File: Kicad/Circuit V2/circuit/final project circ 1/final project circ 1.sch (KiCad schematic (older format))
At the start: 86 parts, among them J1 USB_B_Micro, J10 Conn_01x02_Female, J11 Conn_01x02_Female, J2 Conn_01x01_Female, J3 Conn_01x04_Female, J4 Conn_01x04_Female, J5 Conn_01x03_Female, J6 Conn_01x03_Female, J7 Conn_01x04_Female, J8 Conn_01x02_Female, J9 Conn_01x02_Female, Q1 FDD770N15A, Q2 FDD770N15A, Q3 FDD770N15A, Q4 SS8050-G, Q5 SS8050-G, Q6 2SC1945, SW1 SW_Push, SW2 SW_Push, U1 LTC3895IFE, U2 CP2102N-A01-GQFN28, U3 AZ1117-3.3, U4 USBLC6-4, U5 AZ1117-3.3, U6 ESP32-WROOM-32D, U7 SRD-S-112DM, U8 L2293QTR

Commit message: pcb progress
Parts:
- D6: symbol final-project-circ-1-rescue:PMEG3005EJ-Diode-final-project-circ-1-rescue -> final-project-circ-1-rescue:PMEG3005EJ-Diode-final-project-circ-1-rescue-final-project-circ-1-rescue
- J1: symbol final-project-circ-1-rescue:USB_B_Micro-Connector-final-project-circ-1-rescue -> final-project-circ-1-rescue:USB_B_Micro-Connector-final-project-circ-1-rescue-final-project-circ-1-rescue
- Q1, Q2, Q3: symbol final-project-circ-1-rescue:FDD770N15A-POWSYMBOLS-SDPowSupply-rescue-final-project-circ-1-rescue -> final-project-circ-1-rescue:FDD770N15A-POWSYMBOLS-SDPowSupply-rescue-final-project-circ-1-rescue-final-project-circ-1-r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
- Q4, Q5: symbol final-project-circ-1-rescue:SS8050-G-Custom-final-project-circ-1-rescue -> final-project-circ-1-rescue:SS8050-G-Custom-final-project-circ-1-rescue-final-project-circ-1-rescue
- U1: symbol final-project-circ-1-rescue:LTC3895IFE-POWSYMBOLS-SDPowSupply-rescue-final-project-circ-1-rescue -> final-project-circ-1-rescue:LTC3895IFE-POWSYMBOLS-SDPowSupply-rescue-final-project-circ-1-rescue-final-project-circ-1-r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
- U6: symbol final-project-circ-1-rescue:ESP32-WROOM-32D-RF_Module-final-project-circ-1-rescue -> final-project-circ-1-rescue:ESP32-WROOM-32D-RF_Module-final-project-circ-1-rescue-final-project-circ-1-rescue
- U7: symbol Custom:SRD-S-112DM -> final-project-circ-1-rescue:SRD-S-112DM-Custom
- U8: symbol Custom:L2293QTR -> final-project-circ-1-rescue:L2293QTR-Custom
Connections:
- wire segments 334 -> 335
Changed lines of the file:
@@
 $EndDescr
 $Comp
-L final-project-circ-1-rescue:ESP32-WROOM-32D-RF_Module-final-project-circ-1-rescue U6
+L final-project-circ-1-rescue:ESP32-WROOM-32D-RF_Module-final-project-circ-1-rescue-final-project-circ-1-rescue U6
 U 1 1 61E970AF
 P 25350 15150
@@
 	24400 11300 27400 11300
 $Comp
-L final-project-circ-1-rescue:USB_B_Micro-Connector-final-project-circ-1-rescue J1
+L final-project-circ-1-rescue:USB_B_Micro-Connector-final-project-circ-1-rescue-final-project-circ-1-rescue J1
 U 1 1 61F4B745
 P 18800 10250
@@
 	20800 10050 20800 10450
 $Comp
-L final-project-circ-1-rescue:PMEG3005EJ-Diode-final-project-circ-1-rescue D6
+L final-project-circ-1-rescue:PMEG3005EJ-Diode-final-project-circ-1-rescue-final-project-circ-1-rescue D6
 U 1 1 61F6485B
 P 19800 10050
@@
 $EndComp
 $Comp
-L final-project-circ-1-rescue:SS8050-G-Custom-final-project-circ-1-rescue Q4
+L final-project-circ-1-rescue:SS8050-G-Custom-final-project-circ-1-rescue-final-project-circ-1-rescue Q4
 U 1 1 6208535A
 P 15250 11000
@@
 $EndComp
 $Comp
-L final-project-circ-1-rescue:SS8050-G-Custom-final-project-circ-1-rescue Q5
+L final-project-circ-1-rescue:SS8050-G-Custom-final-project-circ-1-rescue-final-project-circ-1-rescue Q5
 U 1 1 6208695C
 P 15350 12150
@@
 	14750 11000 14950 11000
 $Comp
-L final-project-circ-1-rescue:LTC3895IFE-POWSYMBOLS-SDPowSupply-rescue-final-project-circ-1-rescue U1
+L final-project-circ-1-rescue:LTC3895IFE-POWSYMBOLS-SDPowSupply-rescue-final-project-circ-1-rescue-final-project-circ-1-rescue U1
 U 1 1 61FA0D0E
 P 15250 15900
@@
 	16400 16650 16400 17650
 $Comp
-L final-project-circ-1-rescue:FDD770N15A-POWSYMBOLS-SDPowSupply-rescue-final-project-circ-1-rescue Q3
+L final-project-circ-1-rescue:FDD770N15A-POWSYMBOLS-SDPowSupply-rescue-final-project-circ-1-rescue-final-project-circ-1-rescue Q3
 U 1 1 62007216
 P 17250 20150
@@
 $EndComp
 $Comp
-L final-project-circ-1-rescue:FDD770N15A-POWSYMBOLS-SDPowSupply-rescue-final-project-circ-1-rescue Q2
+L final-project-circ-1-rescue:FDD770N15A-POWSYMBOLS-SDPowSupply-rescue-final-project-circ-1-rescue-final-project-circ-1-rescue Q2
 U 1 1 6200DB26
 P 16750 19150
@@
 $EndComp
 $Comp
-L final-project-circ-1-rescue:FDD770N15A-POWSYMBOLS-SDPowSupply-rescue-final-project-circ-1-rescue Q1
+L final-project-circ-1-rescue:FDD770N15A-POWSYMBOLS-SDPowSupply-rescue-final-project-circ-1-rescue-final-project-circ-1-rescue Q1
 U 1 1 6200EB2C
 P 16450 18150
@@
 	19500 17950 19500 18000
 $Comp
-L Custom:L2293QTR U8
+L final-project-circ-1-rescue:L2293QTR-Custom U8
 U 1 1 62208553
 P 22300 17450
@@
 	21300 18550 22300 18550
 $Comp
-L Custom:SRD-S-112DM U7
+L final-project-circ-1-rescue:SRD-S-112DM-Custom U7
 U 1 1 62253540
 P 19800 17900
@@
 Wire Wire Line
 	21850 18350 21850 19250
+Wire Wire Line
+	15350 12150 15350 12100
 $EndSCHEMATC

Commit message: morr PCB progress
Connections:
- net GND: now also J1.5 (GND); no longer C1.2, C10.1, C11.1, C12.1, C13.1, C2.2, C3.2, C7.1, C8.1, C9.1, D1.2 (A), D2.2 (A), D5.2 (A), Q2.3 (S), R2.2, R3.2, U1.1 (OVLO), U1.12 (GND), U1.15 (GND), U1.19 (DRVUV), U1.39 (GND), U1.9 (GND), U7.1 (GND)
- new net GND1: C1.2, C10.1, C11.1, C12.1, C13.1, C2.2, C3.2, C7.1, C8.1, C9.1, D1.2 (A), D2.2 (A), D5.2 (A), Q2.3 (S), R2.2, R3.2, U1.1 (OVLO), U1.12 (GND), U1.15 (GND), U1.19 (DRVUV), U1.39 (GND), U1.9 (GND), U7.1 (GND)

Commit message: lots of shit
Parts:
- D6: symbol final-project-circ-1-rescue:PMEG3005EJ-Diode-final-project-circ-1-rescue-final-project-circ-1-rescue -> final-project-circ-1-rescue:PMEG3005EJ-Diode-final-project-circ-1-rescue-final-project-circ-1-rescue-final-project-circ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
- J1: symbol final-project-circ-1-rescue:USB_B_Micro-Connector-final-project-circ-1-rescue-final-project-circ-1-rescue -> final-project-circ-1-rescue:USB_B_Micro-Connector-final-project-circ-1-rescue-final-project-circ-1-rescue-final-project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
- Q1, Q2, Q3: symbol final-project-circ-1-rescue:FDD770N15A-POWSYMBOLS-SDPowSupply-rescue-final-project-circ-1-rescue-final-project-circ-1-rescue -> final-project-circ-1-rescue:FDD770N15A-POWSYMBOLS-SDPowSupply-rescue-final-project-circ-1-rescue-final-project-circ-1-rescue-final-project-circ-1-rescue
- Q4, Q5: symbol final-project-circ-1-rescue:SS8050-G-Custom-final-project-circ-1-rescue-final-project-circ-1-rescue -> final-project-circ-1-rescue:SS8050-G-Custom-final-project-circ-1-rescue-final-project-circ-1-rescue-final-project-circ-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
- U1: symbol final-project-circ-1-rescue:LTC3895IFE-POWSYMBOLS-SDPowSupply-rescue-final-project-circ-1-rescue-final-project-circ-1-rescue -> final-project-circ-1-rescue:LTC3895IFE-POWSYMBOLS-SDPowSupply-rescue-final-project-circ-1-rescue-final-project-circ-1-rescue-final-project-circ-1-rescue
- U6: symbol final-project-circ-1-rescue:ESP32-WROOM-32D-RF_Module-final-project-circ-1-rescue-final-project-circ-1-rescue -> final-project-circ-1-rescue:ESP32-WROOM-32D-RF_Module-final-project-circ-1-rescue-final-project-circ-1-rescue-final-pro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
- U7: symbol final-project-circ-1-rescue:SRD-S-112DM-Custom -> final-project-circ-1-rescue:SRD-S-112DM-Custom-final-project-circ-1-rescue
- U8: symbol final-project-circ-1-rescue:L2293QTR-Custom -> final-project-circ-1-rescue:L2293QTR-Custom-final-project-circ-1-rescue

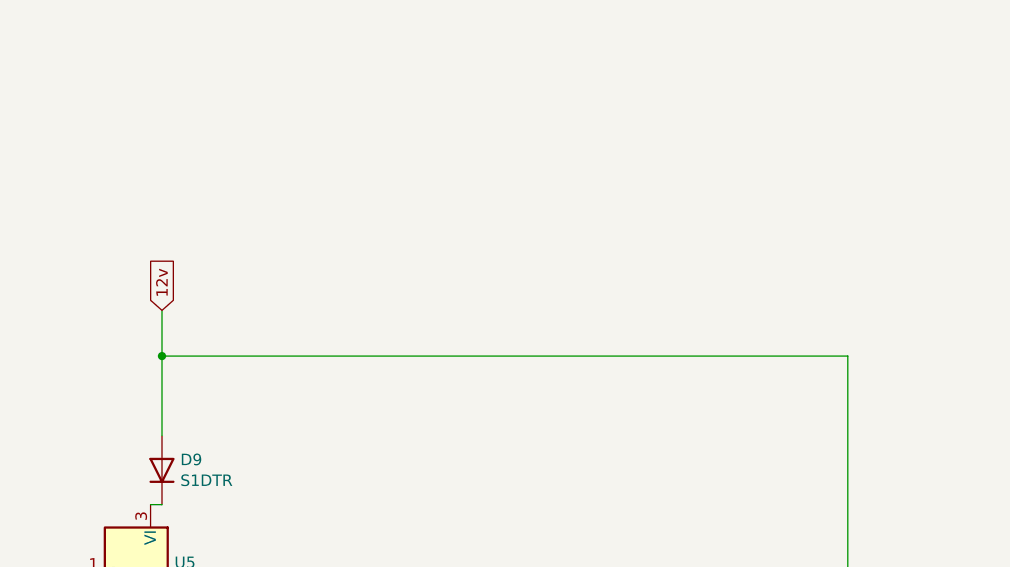
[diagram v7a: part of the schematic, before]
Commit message: added 12 plug for power supplys
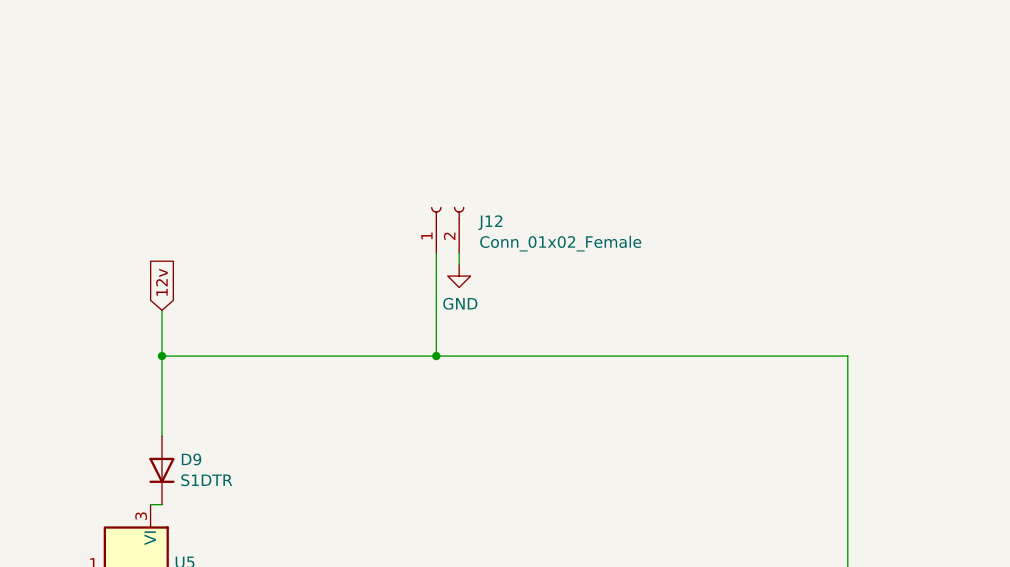
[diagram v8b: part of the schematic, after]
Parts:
- added J12: Conn_01x02_Female, Connector_PinSocket_2.54mm:PinSocket_1x02_P2.54mm_Vertical, symbol Connector:Conn_01x02_Female
- D7: footprint LED_SMD:LED_1206_3216Metric -> Connector_PinSocket_2.54mm:PinSocket_1x02_P2.54mm_Vertical
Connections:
- net 12v: now also J12.1 (Pin_1)
- net GND: now also J12.2 (Pin_2)
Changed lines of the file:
@@
 EESchema Schematic File Version 4
-LIBS:final project circ 1-cache
-EELAYER 29 0
+EELAYER 30 0
 EELAYER END
 $Descr A0 46811 33110
@@
 	24400 11950 24350 11950
 Wire Wire Line
-	24400 11300 27400 11300
+	24400 11300 25600 11300
 $Comp
 L final-project-circ-1-rescue:USB_B_Micro-Connector-final-project-circ-1-rescue-final-project-circ-1-rescue-final-project-circ-1-rescue J1
@@
 F 0 "D7" V 20297 9680 50  0000 L CNN
 F 1 "LED" V 20388 9680 50  0000 L CNN
-F 2 "LED_SMD:LED_1206_3216Metric" H 20350 9600 50  0001 C CNN
+F 2 "Connector_PinSocket_2.54mm:PinSocket_1x02_P2.54mm_Vertical" H 20350 9600 50  0001 C CNN
 F 3 "~" H 20350 9600 50  0001 C CNN
 	1    20350 9600
@@
 	0    1    1    0
 $EndComp
+$Comp
+L Connector:Conn_01x02_Female J12
+U 1 1 6217B9E9
+P 25600 10650
+F 0 "J12" V 25538 10462 50  0000 R CNN
+F 1 "Conn_01x02_Female" V 25447 10462 50  0000 R CNN
+F 2 "Connector_PinSocket_2.54mm:PinSocket_1x02_P2.54mm_Vertical" H 25600 10650 50  0001 C CNN
+F 3 "~" H 25600 10650 50  0001 C CNN
+	1    25600 10650
+	0    -1   -1   0
+$EndComp
+$Comp
+L power:GND #PWR0125
+U 1 1 6217CA20
+P 25700 10900
+F 0 "#PWR0125" H 25700 10650 50  0001 C CNN
+F 1 "GND" H 25705 10727 50  0000 C CNN
+F 2 "" H 25700 10900 50  0001 C CNN
+F 3 "" H 25700 10900 50  0001 C CNN
+	1    25700 10900
+	1    0    0    -1
+$EndComp
+Wire Wire Line
+	25600 10850 25600 11300
+Connection ~ 25600 11300
+Wire Wire Line
+	25600 11300 27400 11300
+Wire Wire Line
+	25700 10850 25700 10900
 $EndSCHEMATC
